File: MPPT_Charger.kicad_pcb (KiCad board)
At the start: 2 copper layers, 95 x 61 mm, 129 parts, among them J1 Solar, J2 Battery, J4 INTERFACE PORT, J6 JTAG/KEYS, J8 Micro_SD_Card_Det_Hirose_DM3AT, J9 IIC RTC, P1 USB-C, Q1 CSD19505KCS, Q2 CSD19505KCS, Q3 CSD19505KCS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

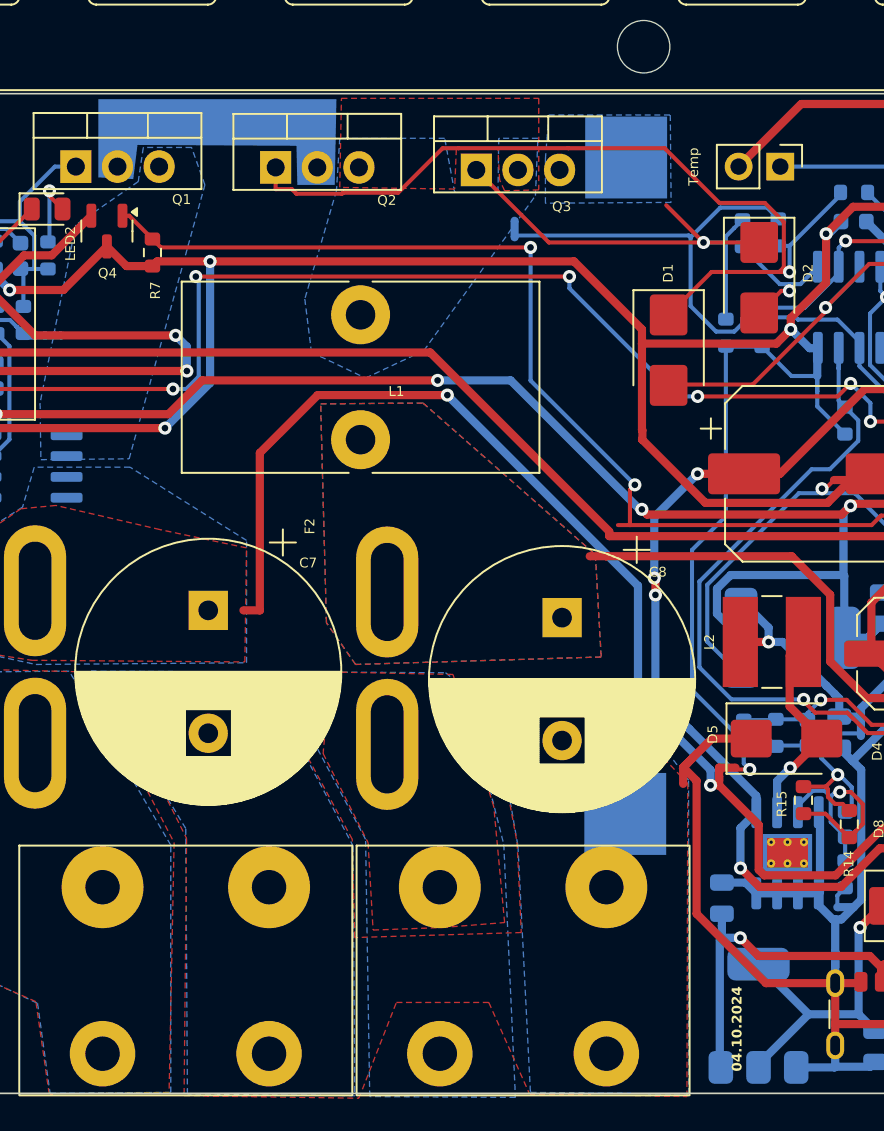
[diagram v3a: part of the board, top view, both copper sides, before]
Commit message: Some Zones were wrong/missing
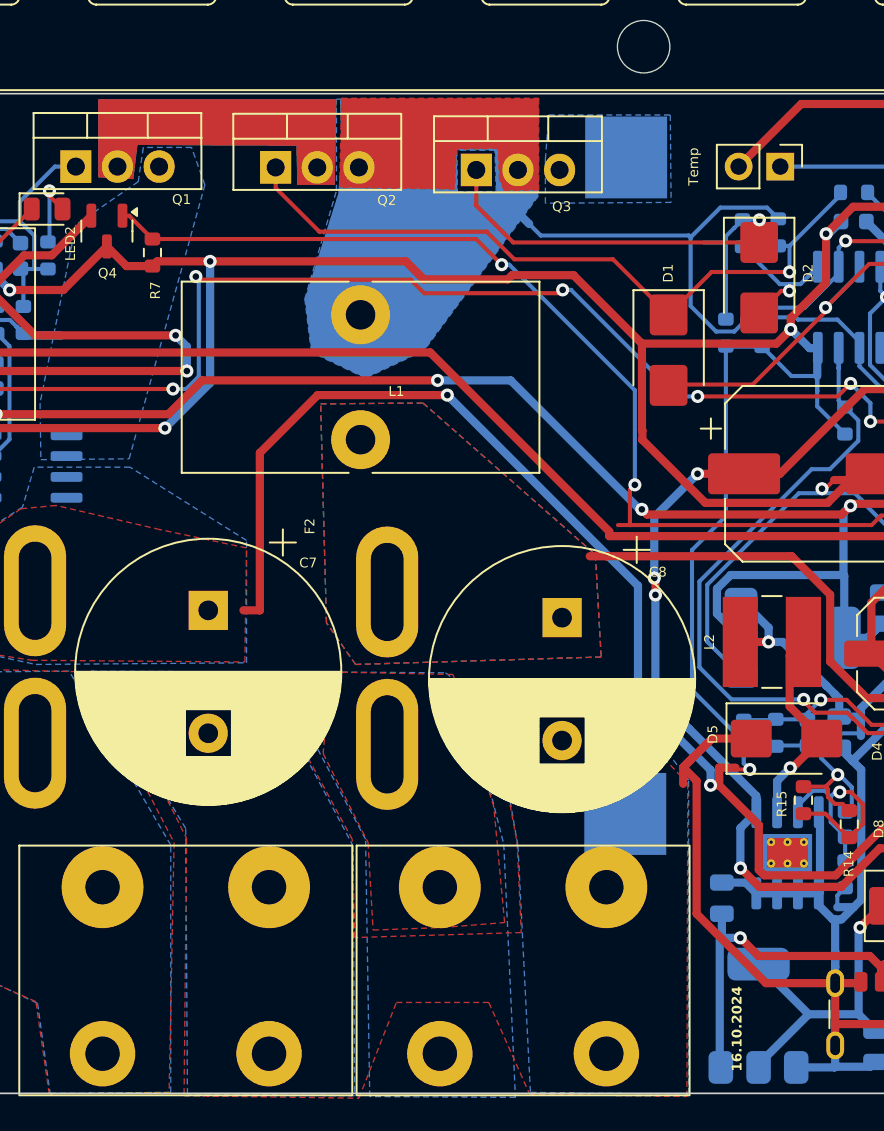
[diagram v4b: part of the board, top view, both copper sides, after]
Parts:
- NT3: value NetTie_2 -> ~
- moved NT4 0.85 mm to (115.6, 101.6), turned to 135 degrees
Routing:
- net Net-(D1-Katode): track 54.7 -> 43.8 mm
- net BCCU: track 106.6 -> 105.3 mm
- net Net-(U7-VS): track 46.1 -> 45.4 mm
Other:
- board text added: "16.10.2024"
- board text removed: "04.10.2024"

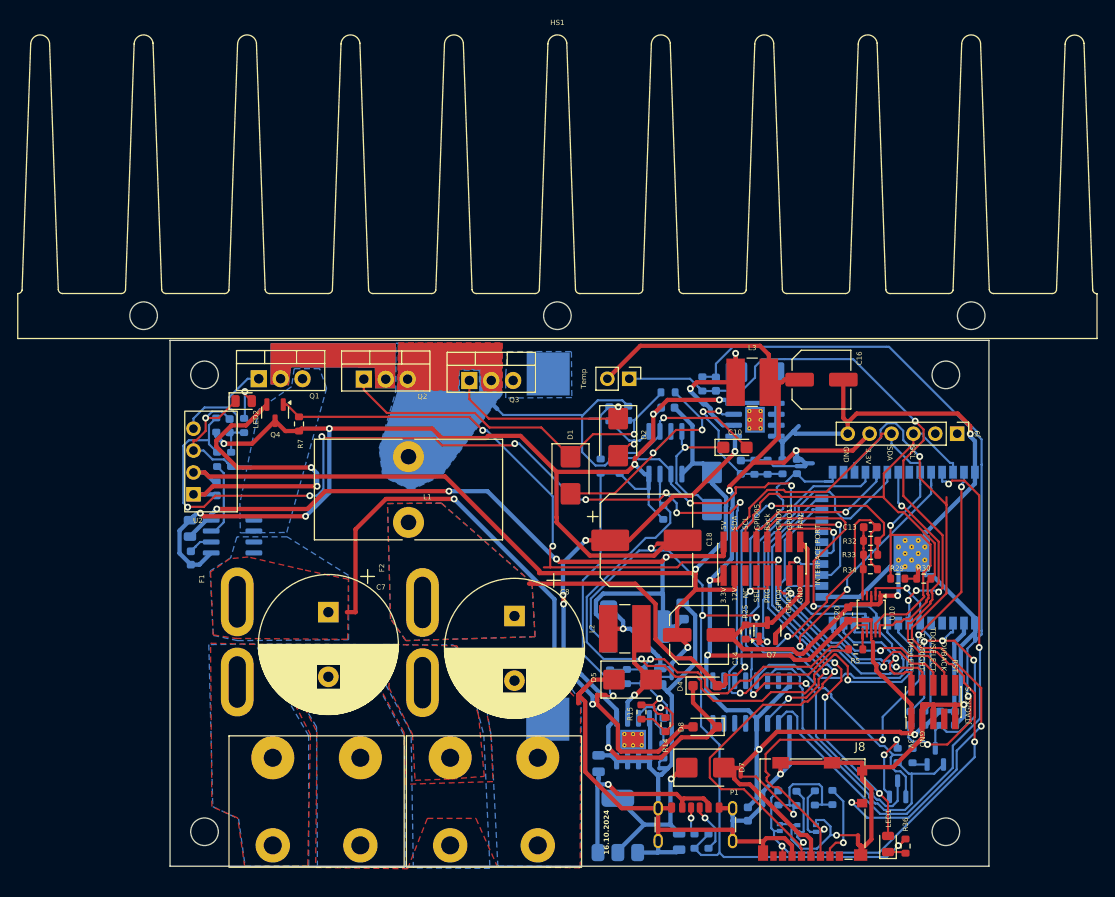
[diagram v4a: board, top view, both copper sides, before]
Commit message: USB-C corrected- I hope Moved more parts topside again
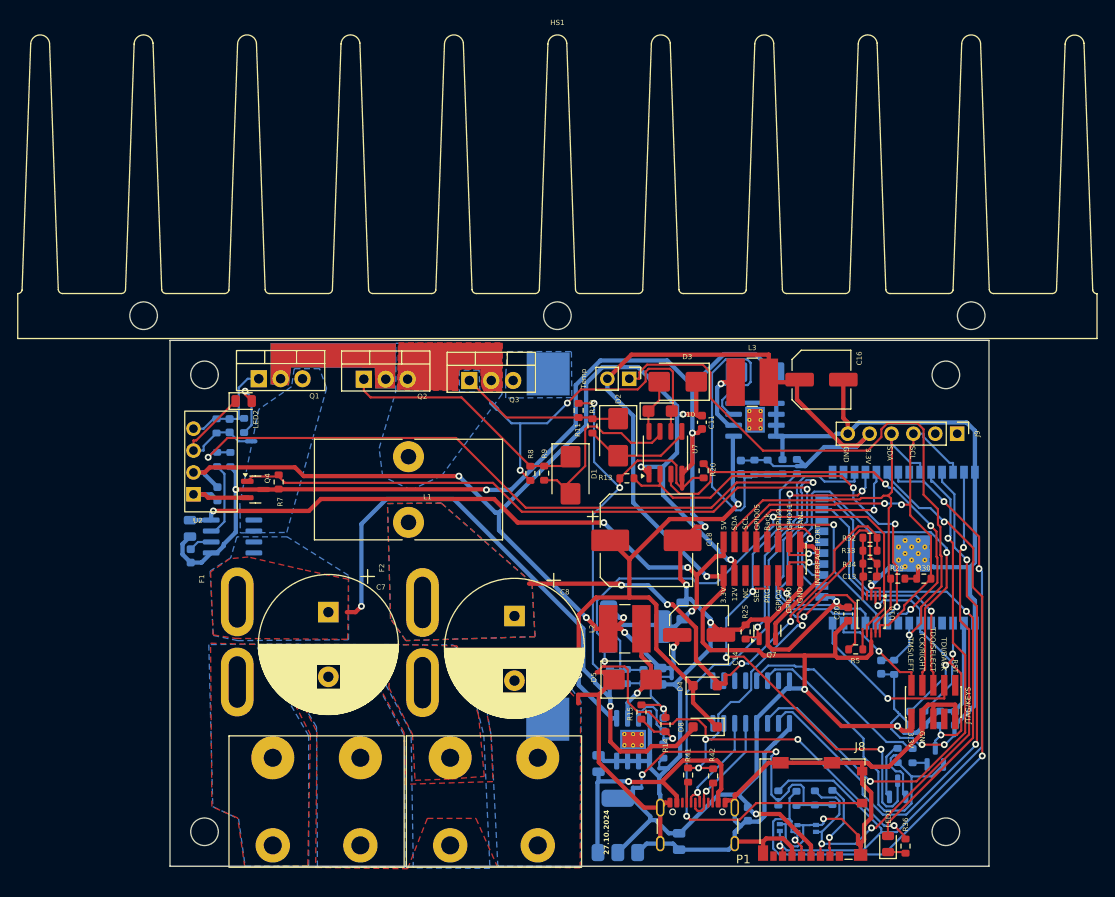
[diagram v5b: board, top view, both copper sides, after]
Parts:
- removed D7: SS310, Diode_SMD:D_SMB
- C11, D3, NT17, R10, R11, R13, R20, R41, R42, R8, R9, U7: moved to F.Cu
- NT8, NT9: moved to B.Cu
- P1: value USB-C -> USB_C_Receptacle_USB2.0_16P; footprint Connector_USB:USB_C_Receptacle_GCT_USB4125-xx-x_6P_TopMnt_Horizontal -> Connector_USB:USB_C_Receptacle_GCT_USB4105-xx-A_16P_TopMnt_Horizontal
- moved R12 39.7 mm to (162.0, 131.9), turned to -90 degrees
- moved C12 38.0 mm to (160.5, 131.9), turned to -90 degrees
- moved R9 17.2 mm to (121.4, 109.4), turned to 90 degrees
- moved NT7 16.5 mm to (128.0, 132.5)
- moved R8 13.3 mm to (119.8, 109.4), turned to -90 degrees
- moved D3 13.3 mm to (136.9, 98.8), turned to 180 degrees
- moved NT8 12.1 mm to (132.2, 145.9), turned to 180 degrees
- moved NT15 11.2 mm to (169.0, 139.3)
- moved C10 9.66 mm to (134.8, 102.2)
- moved Q4 9.20 mm to (87.9, 111.3), turned to 0 degrees
- moved R41 7.71 mm to (138.1, 144.4), turned to 90 degrees
- moved R42 7.59 mm to (141.0, 144.5)
- moved R7 7.13 mm to (90.6, 110.4)
- moved R11 6.95 mm to (125.4, 102.1), turned to 90 degrees
- moved R20 6.72 mm to (139.9, 109.1)
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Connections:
- C22 pad 1: Net-(D7-Katode) -> +3.3V
- U4 pad 2: Net-(D7-Katode) -> +3.3V
- U9 pad 5: Net-(P1-D+) -> Net-(U9-UD+)
- U9 pad 6: Net-(P1-D-) -> Net-(U9-UD-)
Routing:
- net GND_U8: track 84.1 -> 18.8 mm
- net Net-(Q4-D): track 40.3 -> 9.48 mm, vias 2 -> 0
- net A3: track 37.3 -> 65.7 mm
- net DRV_SD: track 79.1 -> 51.5 mm, vias 2 -> 3
- net GND_LP: track 124.7 -> 97.2 mm, vias 5 -> 6
- net GND: track 461.6 -> 434.4 mm, vias 11 -> 8
- net Net-(U6-FB): track 17.6 -> 40.9 mm, vias 2 -> 0
- net DRV_IN: track 72.2 -> 49.0 mm, vias 2 -> 3
- net RX: track 41.0 -> 62.0 mm, vias 4 -> 2
- net Net-(D7-Katode): track 21.0 -> 0.00 mm, vias 1 -> 0
- net KEY_RIGHT: track 28.1 -> 48.7 mm
- net +12V: track 125.2 -> 145.6 mm, vias 3 -> 8
- net Net-(R3-Pad2): track 131.4 -> 111.7 mm, vias 9 -> 3
- net SDA: track 67.1 -> 51.8 mm, vias 1 -> 0
- net Net-(Q1-D): track 16.2 -> 1.49 mm
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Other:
- board text added: "27.10.2024"
- board text removed: "16.10.2024"

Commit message: RxD TxD were wrong :-(
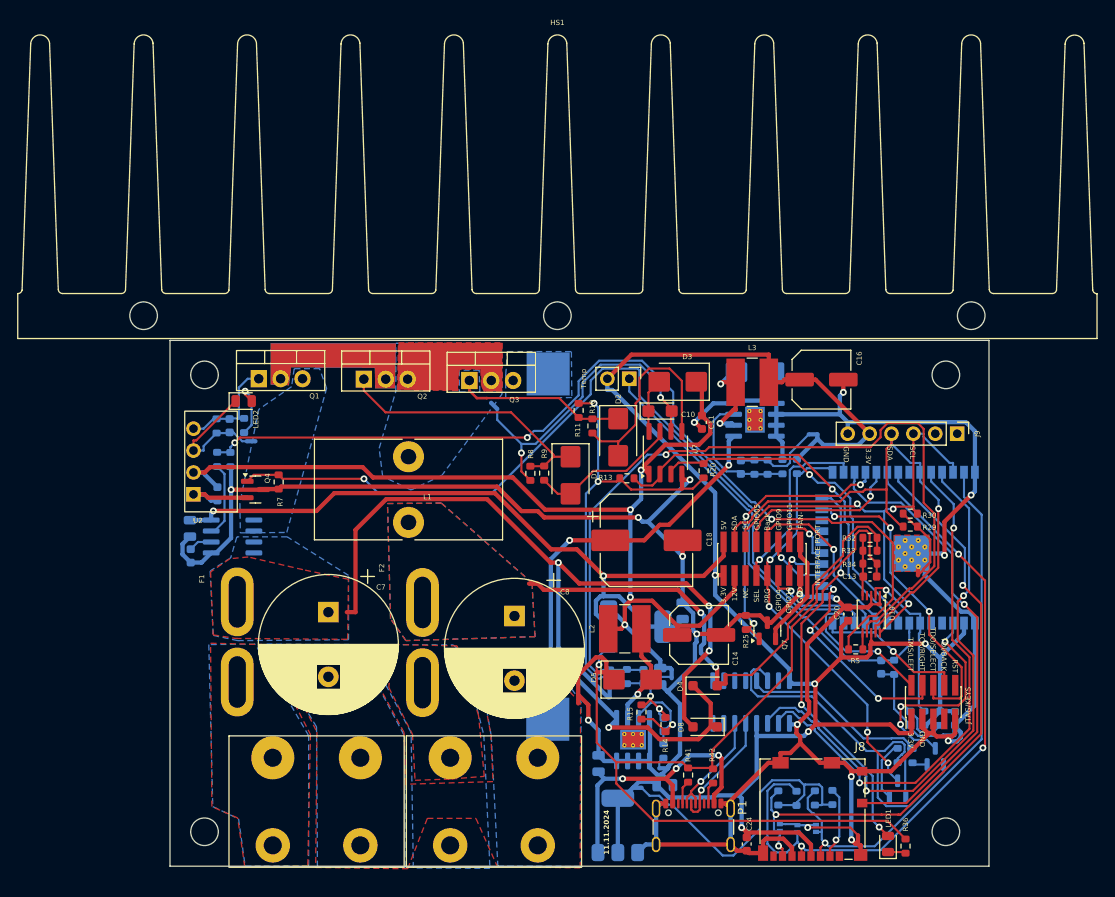
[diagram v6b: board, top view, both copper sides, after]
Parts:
- C24: moved to F.Cu
- moved R30 7.70 mm to (163.9, 114.1)
- moved C22 6.74 mm to (135.4, 145.6), turned to 0 degrees
- moved R29 6.21 mm to (163.9, 115.6)
- moved NT13 3.95 mm to (152.6, 104.9)
- moved C24 3.48 mm to (144.9, 152.4)
- moved R25 1.10 mm to (144.8, 126.7)
- moved P1 0.49 mm to (138.7, 151.4)
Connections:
- J4 pad 7: unconnected-(J4-Pin_7-Pad7) -> GPIO4
- U8 pad 26: SD_DAT1 -> GPIO4
- U9 pad 2: TX -> RX
- U9 pad 3: RX -> TX
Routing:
- net GND: track 434.4 -> 380.1 mm, vias 8 -> 16
- net A3: track 65.7 -> 96.4 mm
- net Net-(U6-FB): track 40.9 -> 15.8 mm
- net KEY_RIGHT: track 48.7 -> 25.3 mm, vias 1 -> 3
- net Utemp: track 76.1 -> 54.2 mm, vias 1 -> 0
- net +12V: track 145.6 -> 123.7 mm, vias 8 -> 4
- net Net-(D8-A): track 69.5 -> 91.1 mm, vias 2 -> 3
- net GPIO4: track 0.00 -> 21.5 mm, vias 0 -> 1
- net SD_DET_B: track 74.6 -> 55.2 mm
- net PRG: track 65.5 -> 47.9 mm, vias 3 -> 4
- net Net-(Q1-D): track 1.49 -> 15.7 mm
- net SD_MISO: track 84.5 -> 71.5 mm
- net Net-(D2-Anode): track 12.9 -> 25.3 mm
- net DRV_SD: track 51.5 -> 40.6 mm, vias 3 -> 1
- net SDA: track 51.8 -> 62.5 mm, vias 0 -> 1
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- added copper zone on F.Cu, net GND
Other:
- board text added: "11.11.2024"
- board text removed: "27.10.2024"

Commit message: Kicad 9.0 + minor changes (some "power" vias)
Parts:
- removed NT5: NetTie_2, NetTie:NetTie-2_SMD_Pad0.5mm
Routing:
- net Net-(D1-Katode): track 31.8 -> 41.5 mm
- net Net-(R3-Pad2): track 110.0 -> 114.4 mm
- net +5V: track 88.3 -> 87.6 mm
- net Net-(Q2-S): vias 0 -> 448
- net Net-(Q1-D): vias 0 -> 174
- net Net-(JP1-B): vias 0 -> 139
- net GND2: vias 0 -> 120
- added copper zone on F.Cu, net Net-(JP1-B)
